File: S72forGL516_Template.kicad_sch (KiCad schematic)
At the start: 259 parts, among them J1 Conn_01x02, J10 Conn_01x01, J11 Conn_01x01, J12 Conn_01x01, J13 Conn_01x01, J14 Conn_01x01, J15 Conn_01x01, J16 Conn_01x01, J17 Conn_01x01, J2 Conn_01x01, J3 Conn_01x01, J4 Conn_01x01, J5 Conn_01x01, J6 Conn_01x01, J7 Conn_01x01, J8 Conn_01x01, J9 Conn_01x01, SW1 SW_PUSH, SW10 SW_PUSH, SW11 SW_PUSH, SW12 SW_PUSH, SW13 SW_PUSH, SW14 SW_PUSH, SW15 SW_PUSH, SW16 SW_PUSH, SW17 SW_PUSH, SW18 SW_PUSH, SW19 SW_PUSH, SW2 SW_PUSH, SW20 SW_PUSH, SW21 SW_PUSH, SW22 SW_PUSH, SW23 SW_PUSH, SW24 SW_PUSH, SW25 SW_PUSH, SW26 SW_PUSH, SW27 SW_PUSH, SW28 SW_PUSH, SW29 SW_PUSH, SW3 SW_PUSH, SW30 SW_PUSH, SW31 SW_PUSH, SW32 SW_PUSH, SW33 SW_PUSH, SW34 SW_PUSH, SW35 SW_PUSH, SW36 SW_PUSH, SW37 SW_PUSH, SW38 SW_PUSH, SW39 SW_PUSH, SW4 SW_PUSH, SW40 SW_PUSH, SW41 SW_PUSH, SW42 SW_PUSH, SW43 SW_PUSH, SW44 SW_PUSH, SW45 SW_PUSH, SW46 SW_PUSH, SW47 SW_PUSH, SW48 SW_PUSH, SW49 SW_PUSH, SW5 SW_PUSH, SW50 SW_PUSH, SW51 SW_PUSH, SW52 SW_PUSH, SW53 SW_PUSH, SW54 SW_PUSH, SW55 SW_PUSH, SW56 SW_PUSH, SW57 SW_PUSH, SW58 SW_PUSH, SW59 SW_PUSH, SW6 SW_PUSH, SW60 SW_PUSH, SW61 SW_PUSH, SW62 SW_PUSH, SW63 SW_PUSH, SW64 SW_PUSH, SW65 SW_PUSH, SW66 SW_PUSH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

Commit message: [FIX] キーの連番、デザインガイドと縦横逆に振ってしまっていた
回路図上、LEDを回転・反転して、アノテーションを振りなおした。
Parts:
- renumbered D46 to D10, D51 to D11, D56 to D12, D61 to D13, D66 to D14, D71 to D15, D76 to D16, D2 to D17, D7 to D18, D12 to D19, D6 to D2, D17 to D20, D22 to D21, D27 to D22, D32 to D23, D37 to D24, D42 to D25, D47 to D26, D52 to D27, D57 to D28, D62 to D29, D11 to D3, D67 to D30, D72 to D31, D77 to D32, D3 to D33, D8 to D34, D13 to D35, D18 to D36, D23 to D37, D28 to D38, D33 to D39, D16 to D4, D38 to D40, D43 to D41, D48 to D42, D53 to D43, D58 to D44, D63 to D45, D68 to D46, D73 to D47, D78 to D48, D4 to D49, D21 to D5, D9 to D50, D14 to D51, D19 to D52, D24 to D53, D29 to D54, D34 to D55, D39 to D56, D44 to D57, D49 to D58, D54 to D59, D26 to D6, D59 to D60, D64 to D61, D69 to D62, D74 to D63, D79 to D64, D5 to D65, D10 to D66, D15 to D67, D20 to D68, D25 to D69, D31 to D7, D30 to D70, D35 to D71, D40 to D72, D45 to D73, D50 to D74, D55 to D75, D60 to D76, D65 to D77, D70 to D78, D75 to D79, D36 to D8, D41 to D9, J14 to J10, J6 to J11, J15 to J12, J7 to J13, J16 to J14, J8 to J15, J17 to J16, J9 to J17, J10 to J2, J2 to J3, J11 to J4, J3 to J5, J12 to J6, J4 to J7, J13 to J8, J5 to J9, SW46 to SW10, SW51 to SW11, SW56 to SW12, SW61 to SW13, SW66 to SW14, SW71 to SW15, SW76 to SW16, SW2 to SW17, SW7 to SW18, SW12 to SW19, SW6 to SW2, SW17 to SW20, SW22 to SW21, SW27 to SW22, SW32 to SW23, SW37 to SW24, SW42 to SW25, SW47 to SW26, SW52 to SW27, SW57 to SW28, SW62 to SW29, SW11 to SW3, SW67 to SW30, SW72 to SW31, SW77 to SW32, SW3 to SW33, SW8 to SW34, SW13 to SW35, SW18 to SW36, SW23 to SW37, SW28 to SW38, SW33 to SW39, SW16 to SW4, SW38 to SW40, SW43 to SW41, SW48 to SW42, SW53 to SW43, SW58 to SW44, SW63 to SW45, SW68 to SW46, SW73 to SW47, SW78 to SW48, SW4 to SW49, SW21 to SW5, SW9 to SW50, SW14 to SW51, SW19 to SW52, SW24 to SW53, SW29 to SW54, SW34 to SW55, SW39 to SW56, SW44 to SW57, SW49 to SW58, SW54 to SW59, SW26 to SW6, SW59 to SW60, SW64 to SW61, SW69 to SW62, SW74 to SW63, SW79 to SW64, SW5 to SW65, SW10 to SW66, SW15 to SW67, SW20 to SW68, SW25 to SW69, SW31 to SW7, SW30 to SW70, SW35 to SW71, SW40 to SW72, SW45 to SW73, SW50 to SW74, SW55 to SW75, SW60 to SW76, SW65 to SW77, SW70 to SW78, SW75 to SW79, SW36 to SW8, SW41 to SW9
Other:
- moved on the sheet: D1, D10, D11, D12, D13, D14, D15, D16, D17, D18, D19, D2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

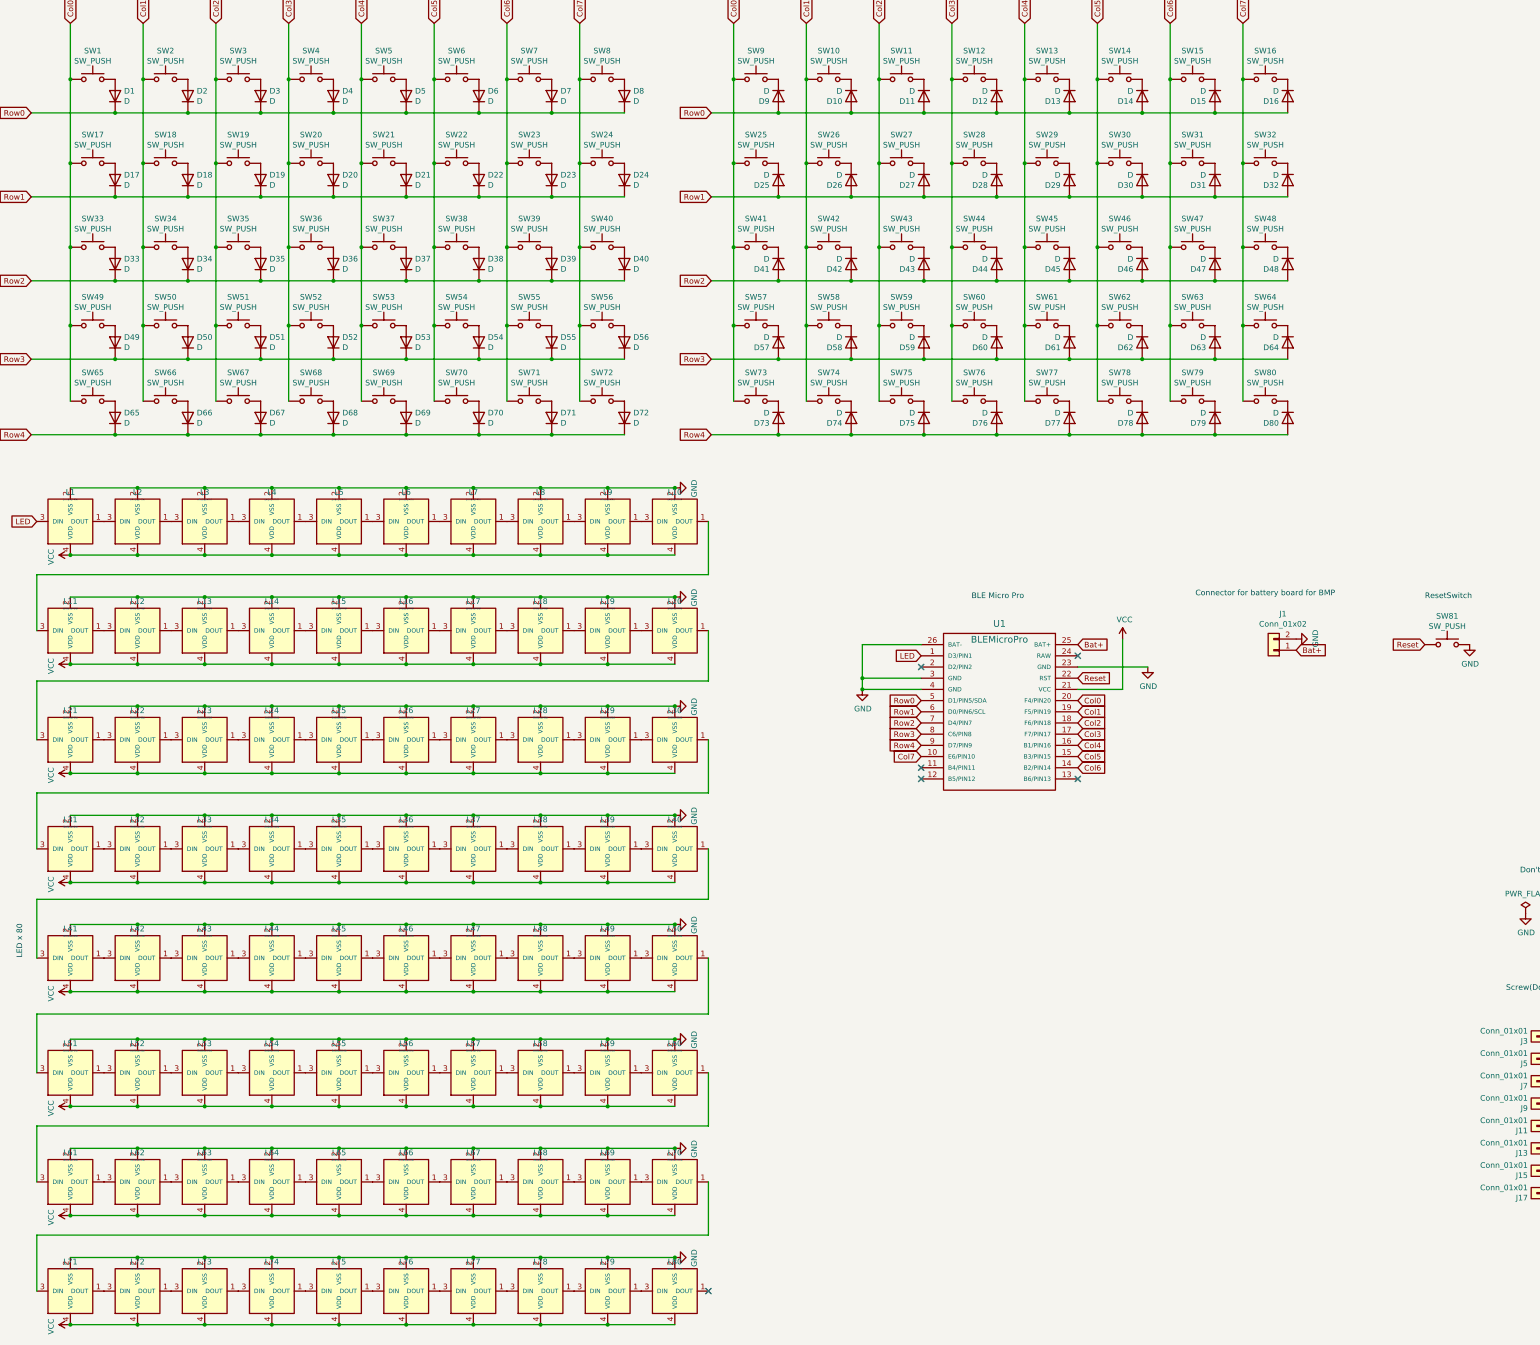
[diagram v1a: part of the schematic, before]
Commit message: キースイッチとLEDの数を調整
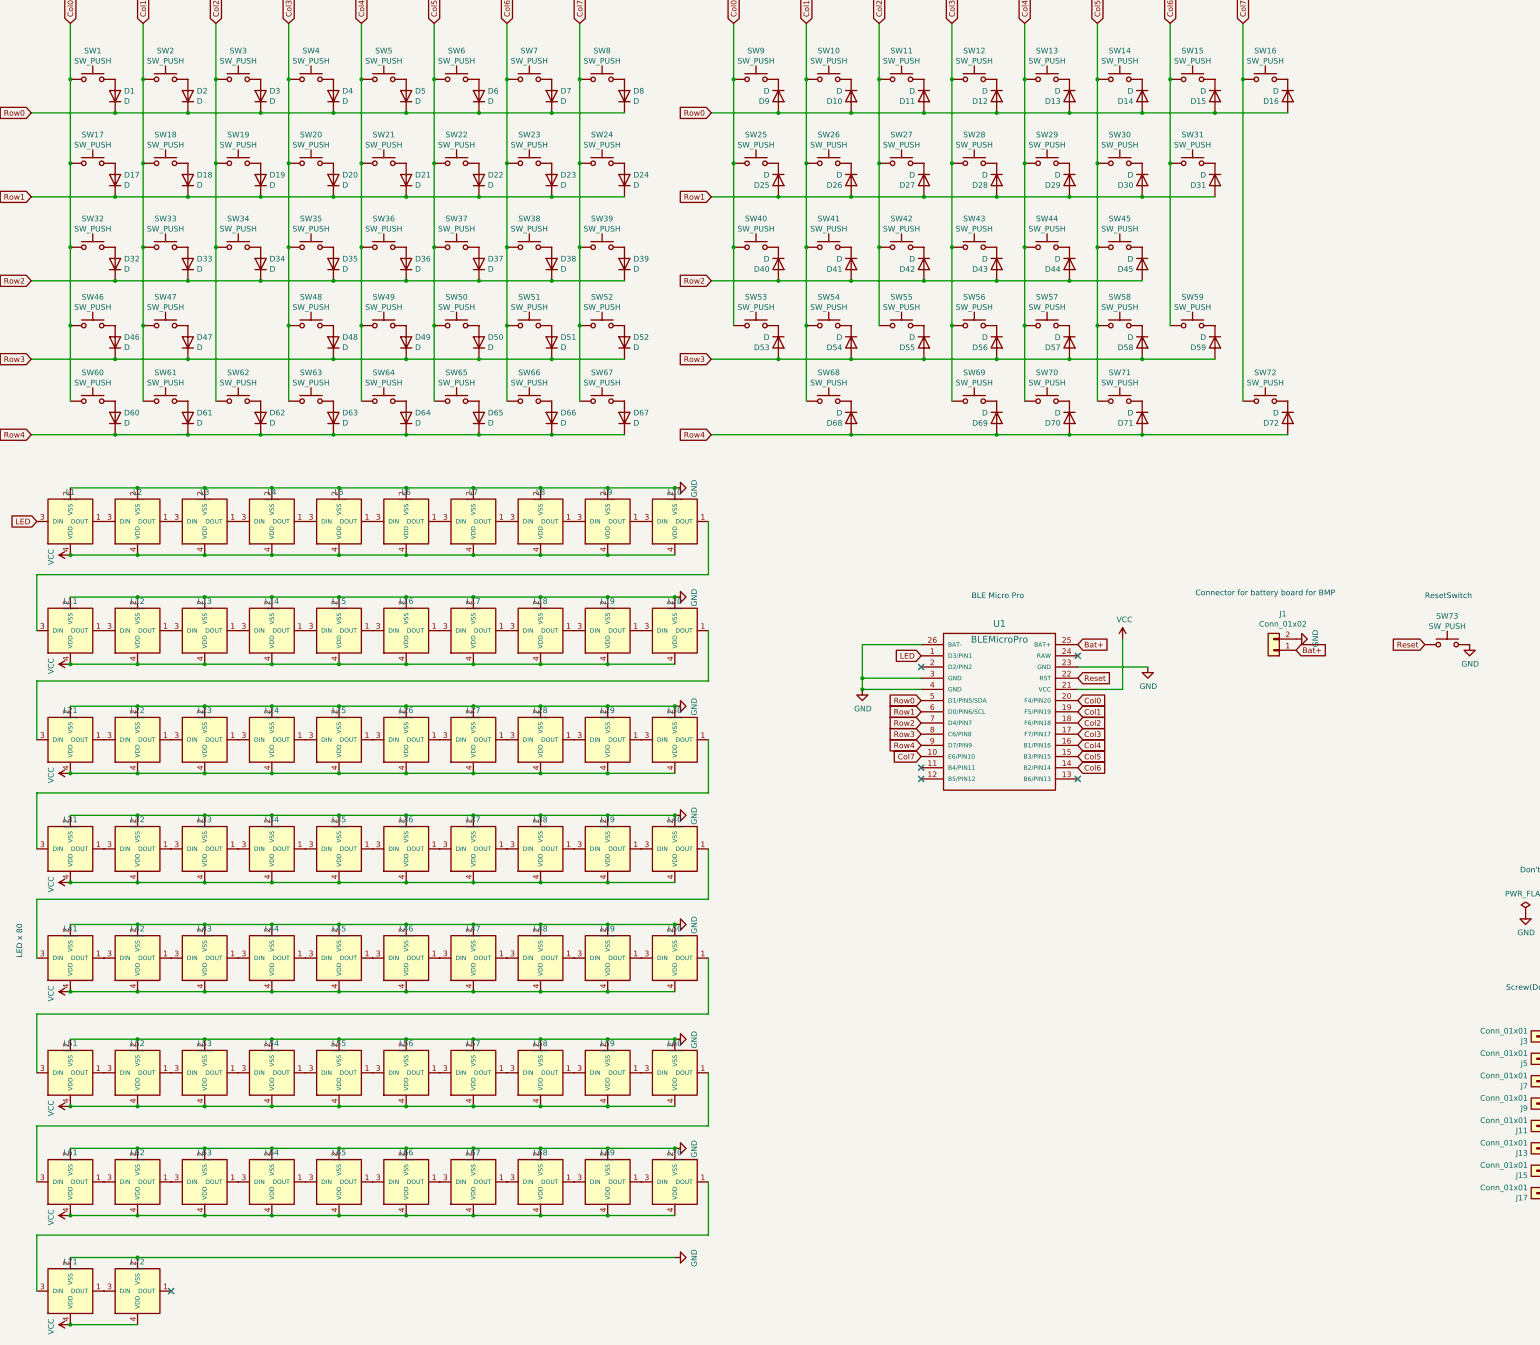
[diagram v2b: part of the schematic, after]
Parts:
- removed D32, D47, D48, D51, D64, D73, D75, D79: D, kbd_Parts:Diode_TH_SMD, symbol Device:D
- removed L73, L74, L75, L76, L77, L78, L79, L80: SK6812MINI, kbd_Parts:LED_SK6812MINI-E_BL, symbol Salicylic_kbd:LED_SK6812MINI-E
- removed SW32, SW47, SW48, SW51, SW64, SW73, SW75, SW79: SW_PUSH, kbd_SW:CherryMX_Hotswap_1u, symbol Switch:SW_Push
- renumbered D33 to D32, D34 to D33, D35 to D34, D36 to D35, D37 to D36, D38 to D37, D39 to D38, D40 to D39, D41 to D40, D42 to D41, D43 to D42, D44 to D43, D45 to D44, D46 to D45, D49 to D46, D50 to D47, D52 to D48, D53 to D49, D54 to D50, D55 to D51, D56 to D52, D57 to D53, D58 to D54, D59 to D55, D60 to D56, D61 to D57, D62 to D58, D63 to D59, D65 to D60, D66 to D61, D67 to D62, D68 to D63, D69 to D64, D70 to D65, D71 to D66, D72 to D67, D74 to D68, D76 to D69, D77 to D70, D78 to D71, D80 to D72, SW33 to SW32, SW34 to SW33, SW35 to SW34, SW36 to SW35, SW37 to SW36, SW38 to SW37, SW39 to SW38, SW40 to SW39, SW41 to SW40, SW42 to SW41, SW43 to SW42, SW44 to SW43, SW45 to SW44, SW46 to SW45, SW49 to SW46, SW50 to SW47, SW52 to SW48, SW53 to SW49, SW54 to SW50, SW55 to SW51, SW56 to SW52, SW57 to SW53, SW58 to SW54, SW59 to SW55, SW60 to SW56, SW61 to SW57, SW62 to SW58, SW63 to SW59, SW65 to SW60, SW66 to SW61, SW67 to SW62, SW68 to SW63, SW69 to SW64, SW70 to SW65, SW71 to SW66, SW72 to SW67, SW74 to SW68, SW76 to SW69, SW77 to SW70, SW78 to SW71, SW80 to SW72, SW81 to SW73

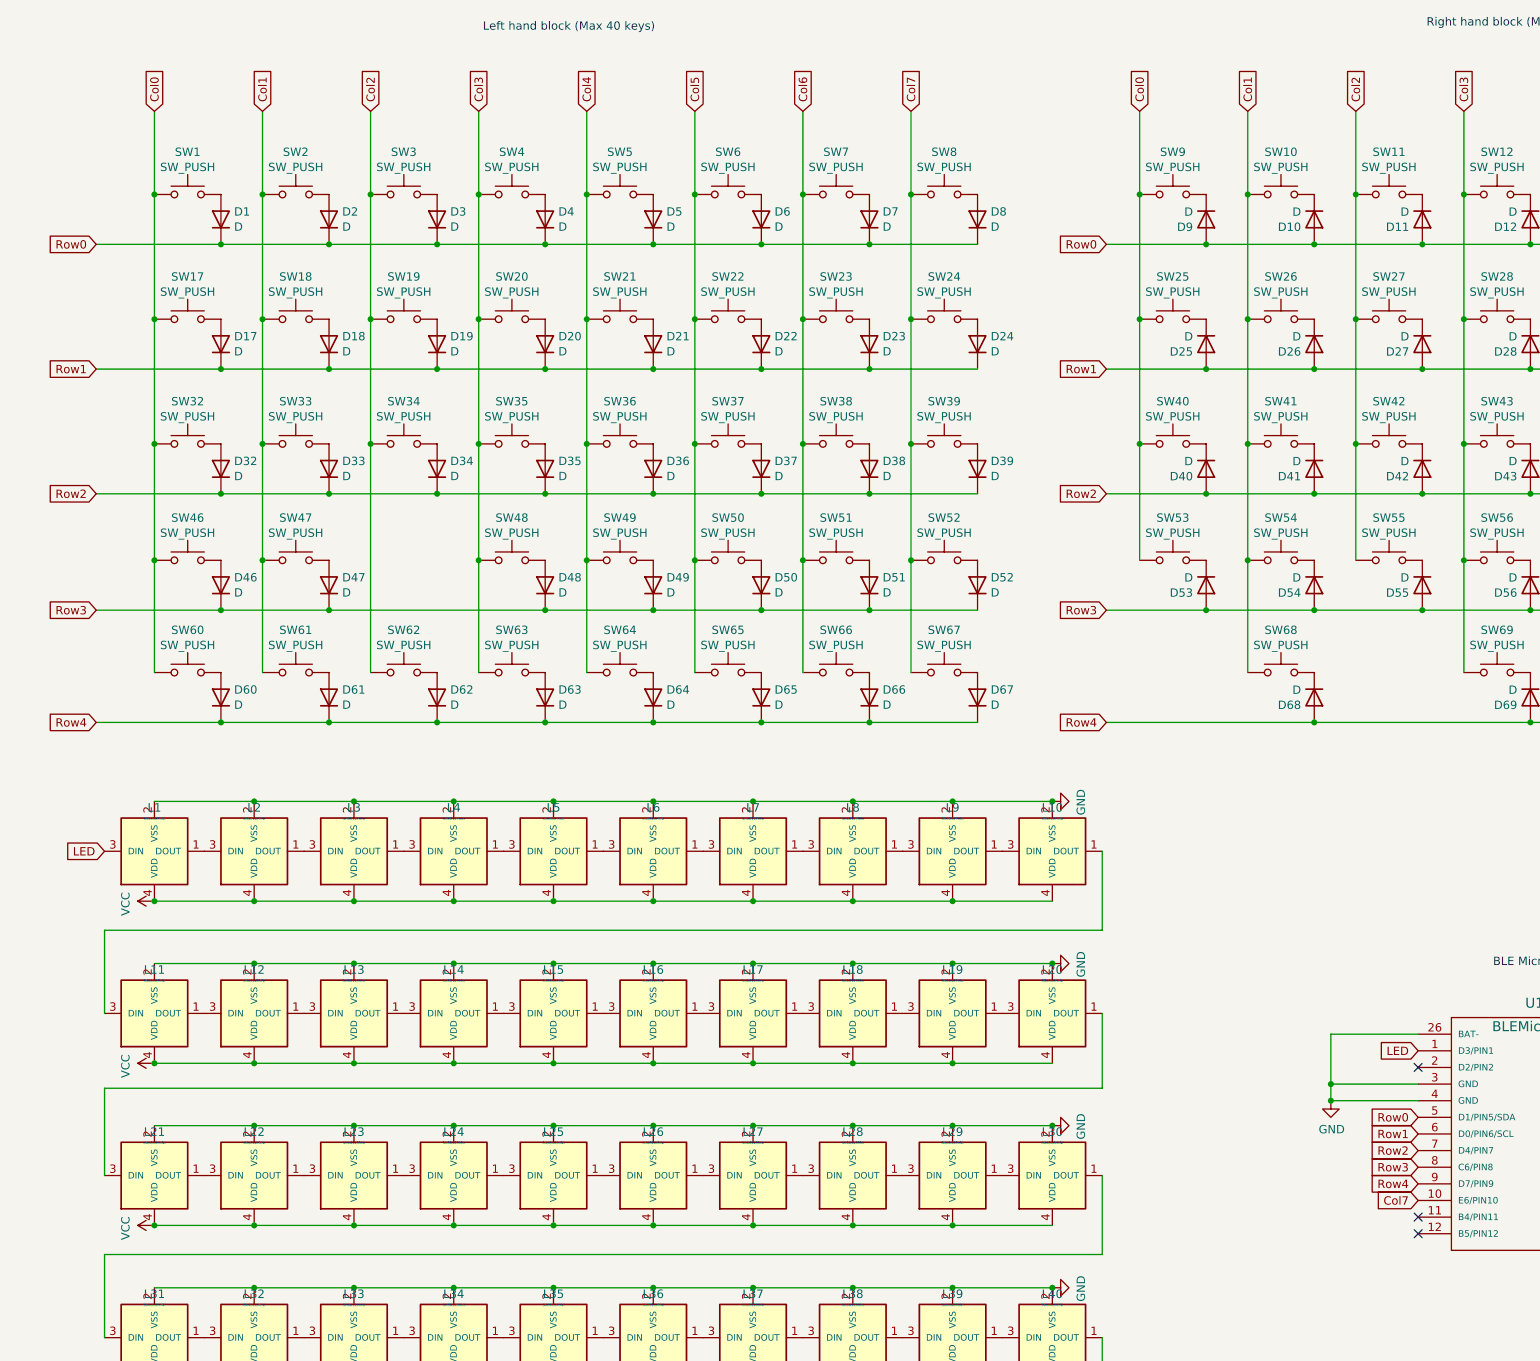
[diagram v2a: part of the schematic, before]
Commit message: 左上隅をロータリーエンコーダにしてみた
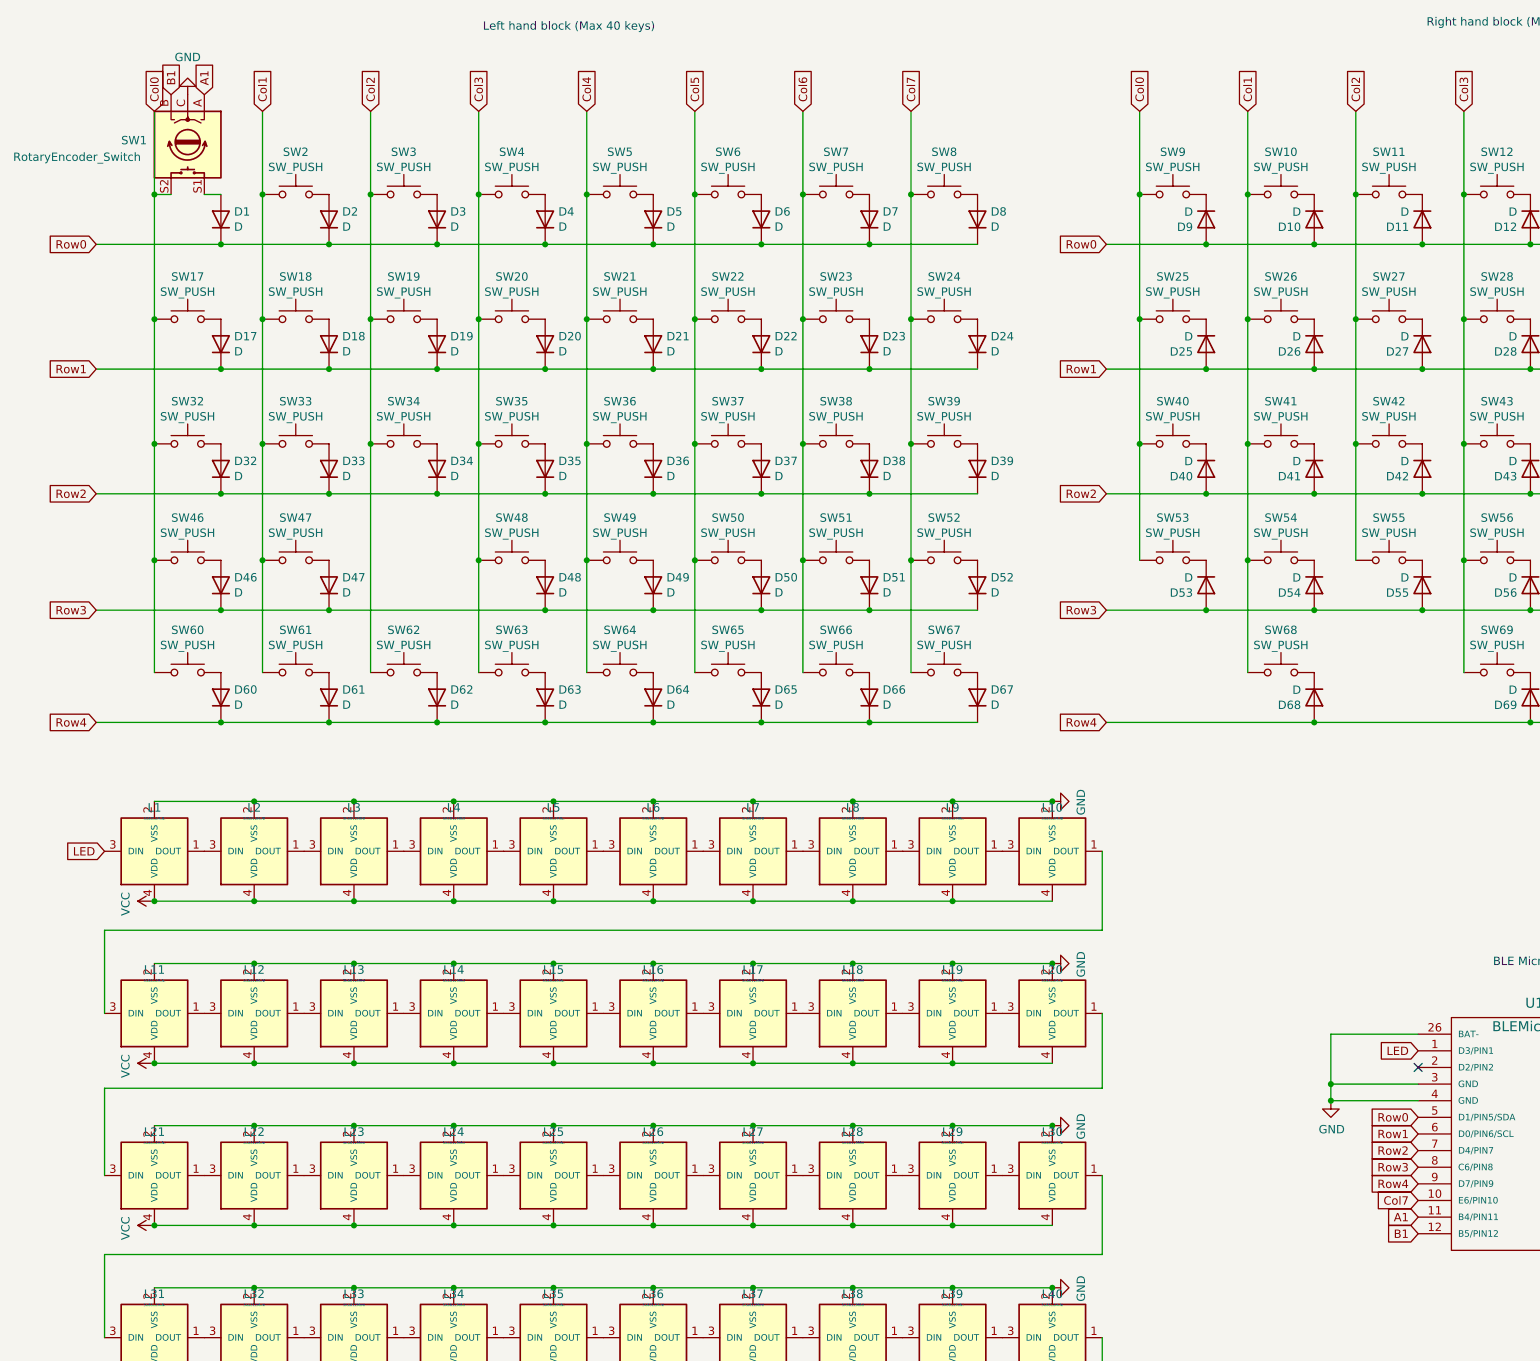
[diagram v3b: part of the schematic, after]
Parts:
- removed SW1: SW_PUSH, kbd_SW:CherryMX_Hotswap_1u, symbol Switch:SW_Push
- added SW1: RotaryEncoder_Switch, symbol Device:RotaryEncoder_Switch
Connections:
- net Col0: now also SW1.S2
- net GND: now also SW1.C
- net A1: now reaches U1.11 (B4/PIN11)
- net A1: now also SW1.A
- net B1: now reaches U1.12 (B5/PIN12)
- net B1: now also SW1.B
- net at D1.2 (A): now also SW1.S1
- no-connect marks 6 -> 4
